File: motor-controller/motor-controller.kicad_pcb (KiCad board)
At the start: 2 copper layers, 65.4 x 35.6 mm, 21 parts, among them J1 Molex 172043-0201 R/A, J2 Molex 172043-0302 R/A, J3 MCU-IO, U1 DRV10983PWP

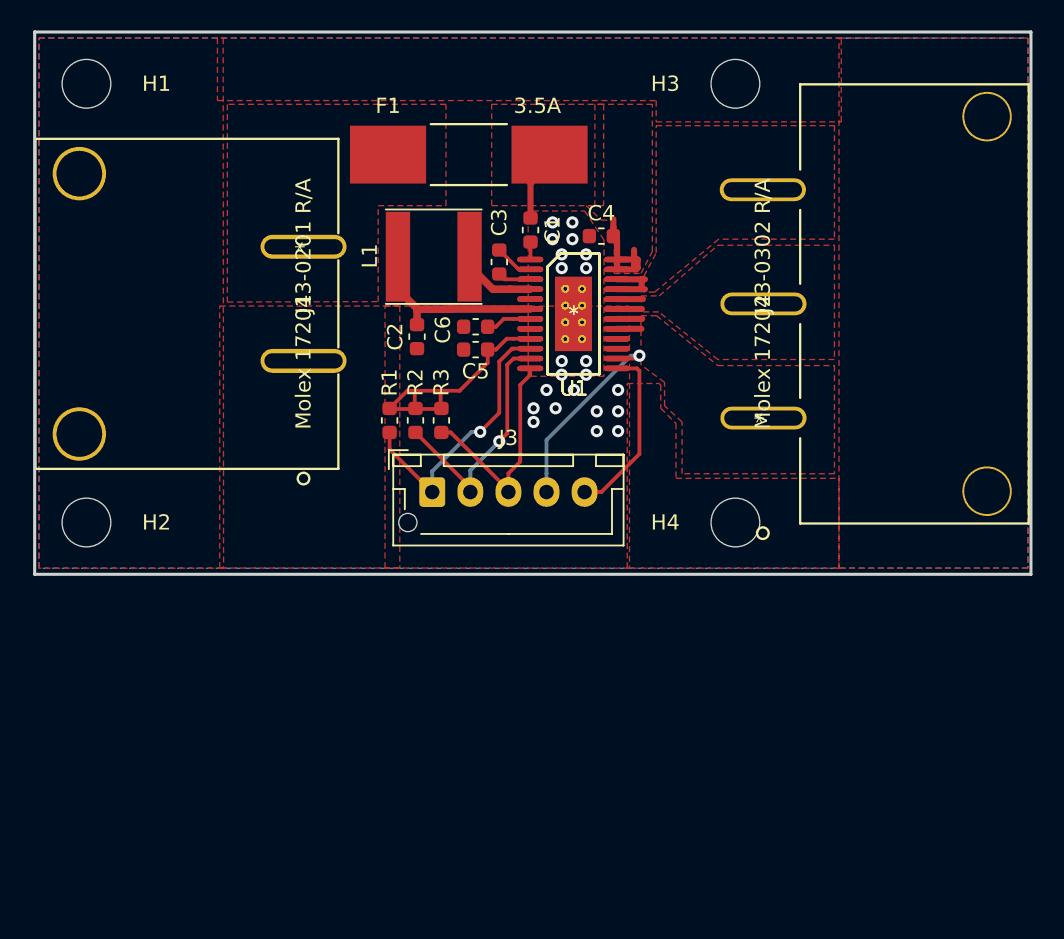
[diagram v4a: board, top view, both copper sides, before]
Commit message: Thermal vias connected to pad in driver IC footprint; added PCB dimensions, adjusted fuse pours.
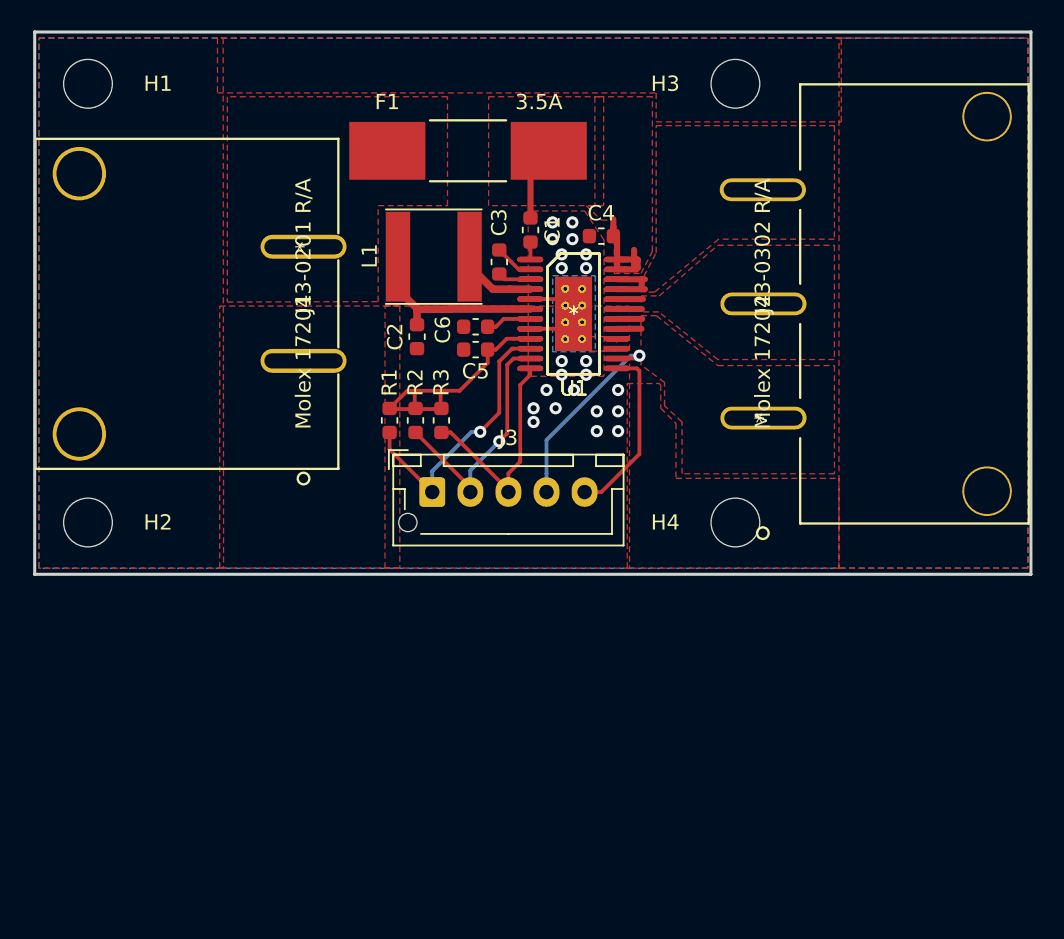
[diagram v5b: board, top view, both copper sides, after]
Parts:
- removed the U1 at (152.4, 103.5) (x3)
- added U1 (x3): DRV10983PWP, custom:PWP0024B, F.Cu at (152.4, 103.5)
- moved F1 0.25 mm to (145.4, 92.8)
- moved H1 0.10 mm to (120.5, 88.4)
- moved H2 0.10 mm to (120.5, 117.2)
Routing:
- net GND: track 0.00 -> 6.51 mm
- net VCC: track 11.8 -> 12.7 mm

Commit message: Prelayout modifications; changed 7-pin connector pinout to permit tighter layout.
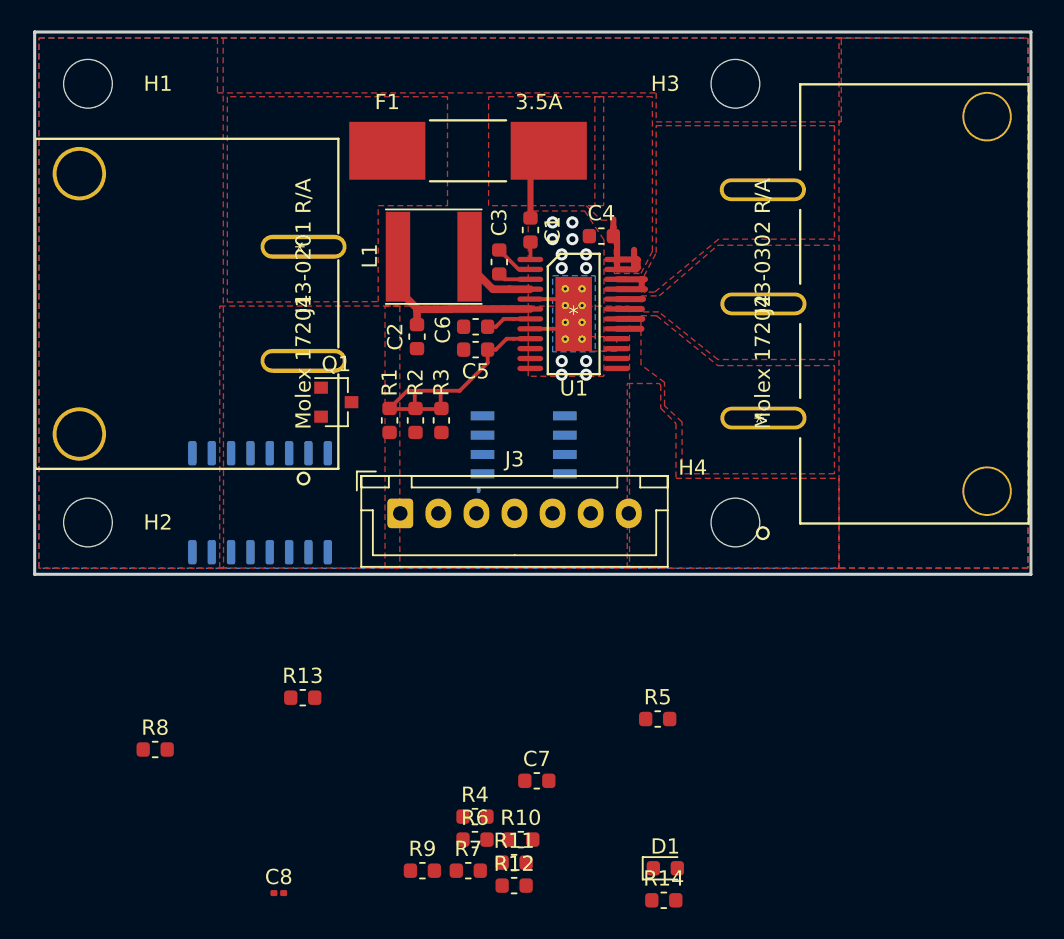
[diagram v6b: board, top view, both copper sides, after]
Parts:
- removed the U1 at (152.4, 103.5) (x3)
- added C7: C, Capacitor_SMD:C_0603_1608Metric, F.Cu at (150.0, 134.2)
- added C8: C, Capacitor_SMD:C_0201_0603Metric, F.Cu at (133.0, 141.5)
- added D1: LED, LED_SMD:LED_0603_1608Metric, F.Cu at (158.4, 139.9)
- added Q1: 2N3904, Package_TO_SOT_SMD:SOT-23, F.Cu at (136.8, 109.3)
- added R10: 4.7k, Resistor_SMD:R_0603_1608Metric, F.Cu at (148.9, 138.0)
- added R11: 4.7k, Resistor_SMD:R_0603_1608Metric, F.Cu at (148.5, 139.5)
- added R12: 4.7k, Resistor_SMD:R_0603_1608Metric, F.Cu at (148.5, 141.0)
- added R13: 4.7k, Resistor_SMD:R_0603_1608Metric, F.Cu at (134.6, 128.7)
- added R14: 220, Resistor_SMD:R_0603_1608Metric, F.Cu at (158.3, 142.0)
- added R4: 75, Resistor_SMD:R_0603_1608Metric, F.Cu at (145.9, 136.5)
- added R5: 200, Resistor_SMD:R_0603_1608Metric, F.Cu at (157.9, 130.1)
- added R6: 200, Resistor_SMD:R_0603_1608Metric, F.Cu at (145.9, 138.0)
- added R7: 200, Resistor_SMD:R_0603_1608Metric, F.Cu at (145.5, 140.1)
- added R8: 75, Resistor_SMD:R_0603_1608Metric, F.Cu at (124.9, 132.1)
- added R9: 1k, Resistor_SMD:R_0603_1608Metric, F.Cu at (142.5, 140.1)
- added U1: DRV10983PWP, custom:PWP0024B, F.Cu at (152.4, 103.5)
- added U2: TLP291-4, Package_SO:SOIC-16_4.55x10.3mm_P1.27mm, B.Cu at (131.8, 115.9)
- added U3: SI8600AC, Package_SO:SOIC-8_3.9x4.9mm_P1.27mm, B.Cu at (149.1, 112.1)
- J3: footprint Connector_JST:JST_XH_B05B-XH-AM_1x05_P2.50mm_Vertical -> Connector_JST:JST_XH_B07B-XH-A_1x07_P2.50mm_Vertical
- moved J3 2.52 mm to (141.0, 116.6)
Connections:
- J3 pad 1: Net-(J3-Pad1) -> /SPEED-uC
- J3 pad 2: Net-(J3-Pad2) -> /FG-uC
- J3 pad 3: Net-(J3-Pad3) -> /DIR-uC
- J3 pad 4: /DIR -> +5V
- J3 pad 5: /SPEED -> GNDD
- R1 pad 2: Net-(J3-Pad1) -> /SDA-MTR
- R2 pad 2: Net-(J3-Pad2) -> /SCL-MTR
- R3 pad 2: Net-(J3-Pad3) -> /FG-MTR
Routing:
- net Net-(J3-Pad1): track 18.2 -> 0.00 mm, vias 1 -> 0
- net Net-(J3-Pad2): track 16.6 -> 0.12 mm, vias 1 -> 0
- net Net-(J3-Pad3): track 14.8 -> 0.00 mm
- net /DIR: track 13.4 -> 0.00 mm, vias 1 -> 0
- net /SPEED: track 11.6 -> 0.00 mm
- net GND: vias 22 -> 12

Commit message: Added in isolator traces and placed resistors; need to add ground planes and tweak layout.
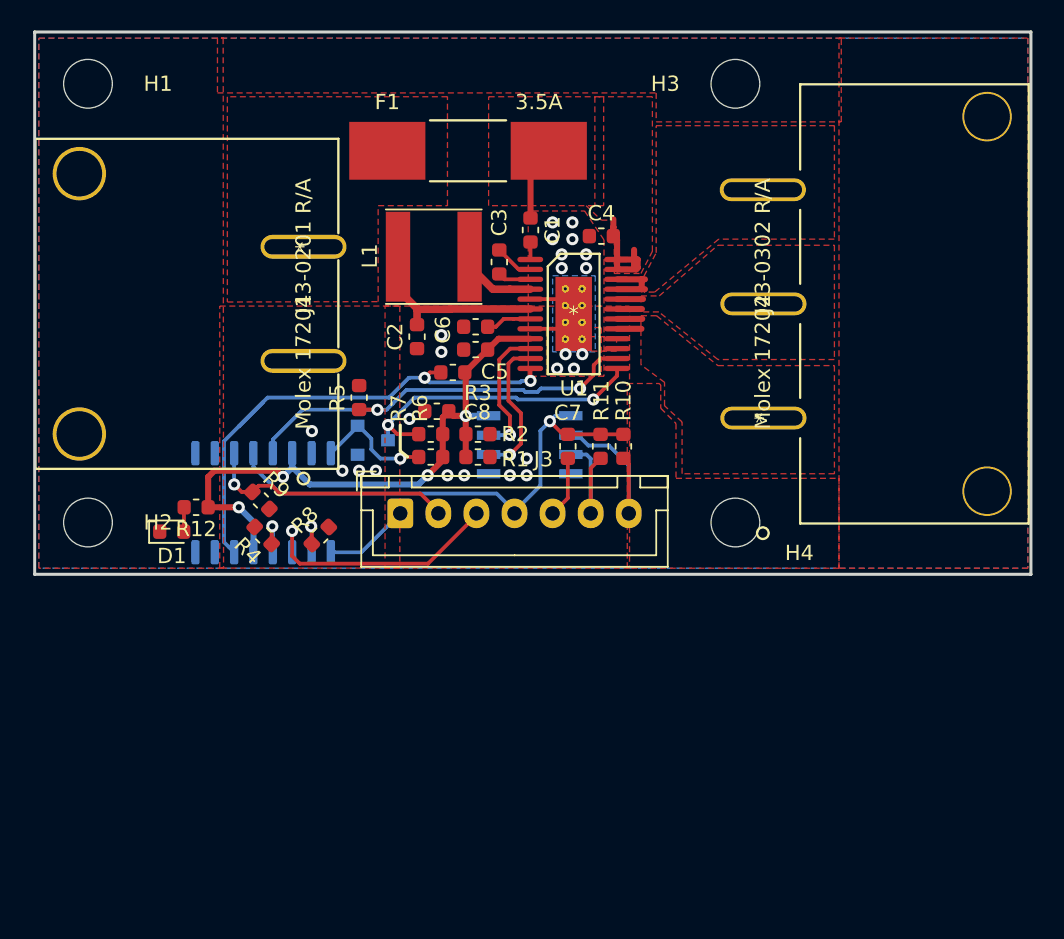
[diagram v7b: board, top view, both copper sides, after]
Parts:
- removed R13: 4.7k, Resistor_SMD:R_0603_1608Metric
- removed R14: 220, Resistor_SMD:R_0603_1608Metric
- C8: footprint Capacitor_SMD:C_0201_0603Metric -> Capacitor_SMD:C_0603_1608Metric
- Q1: moved to B.Cu
- R12: value 4.7k -> 220
- moved D1 39.2 mm to (126.0, 117.8)
- moved C8 33.3 mm to (143.4, 109.9), turned to 180 degrees
- moved R12 32.4 mm to (127.6, 116.2), turned to 180 degrees
- moved R5 28.8 mm to (138.3, 109.0), turned to 90 degrees
- moved R11 27.9 mm to (154.2, 112.2), turned to 270 degrees
- moved R7 27.3 mm to (143.0, 112.9), turned to 180 degrees
- moved R6 26.8 mm to (143.0, 111.4), turned to 180 degrees
- moved R10 26.7 mm to (155.7, 112.2), turned to 270 degrees
- moved R9 26.5 mm to (131.8, 115.8), turned to 315 degrees
- moved R4 23.1 mm to (132.0, 118.0), turned to 135 degrees
- moved C7 22.0 mm to (152.0, 112.2), turned to 270 degrees
- moved R8 17.7 mm to (135.8, 118.0), turned to 45 degrees
- moved R1 6.28 mm to (146.1, 112.9), turned to 0 degrees
- moved R2 4.20 mm to (146.1, 111.4), turned to 0 degrees
- moved Q1 3.47 mm to (139.2, 111.8)
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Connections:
- R12 pad 2: /SCL-MTR -> Net-(D1-Pad2)
- U2 pad 11: /DIR-MTR -> /FG-uC
- U2 pad 12: +3V3 -> +5V
- U2 pad 13: /FG-uC -> /DIR-MTR
- U2 pad 14: +5V -> +3V3
- U2 pad 3: +3V3 -> /DIR-uC
- U2 pad 4: /FG-MTR -> Net-(R4-Pad1)
- U2 pad 5: /DIR-uC -> +3V3
- U2 pad 6: Net-(R4-Pad1) -> /FG-MTR
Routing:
- net /FG-MTR: track 0.00 -> 34.2 mm, vias 0 -> 2
- net +5V: track 0.00 -> 33.0 mm, vias 0 -> 1
- net /DIR-MTR: track 0.00 -> 27.4 mm, vias 0 -> 2
- net +3V3: track 17.5 -> 43.6 mm, vias 0 -> 4
- net /SPEED-MTR: track 0.00 -> 20.3 mm, vias 0 -> 2
- net /DIR-uC: track 0.00 -> 16.8 mm, vias 0 -> 1
- net /FG-uC: track 0.00 -> 16.6 mm, vias 0 -> 1
- net /SCL-uC: track 0.00 -> 11.5 mm
- net /SDA-MTR: track 0.00 -> 9.62 mm, vias 0 -> 1
- net /SCL-MTR: track 0.00 -> 9.00 mm, vias 0 -> 1
- net /SDA-uC: track 0.00 -> 8.89 mm
- net Net-(Q1-Pad2): track 0.00 -> 7.88 mm, vias 0 -> 1
- net /SPEED-uC: track 0.00 -> 5.66 mm
- net GNDD: track 0.00 -> 4.03 mm
- net Net-(R4-Pad1): track 0.00 -> 2.89 mm, vias 0 -> 1
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
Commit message: Added in uC-side ground planes; adjusted isolator trace layouts to pass DRC
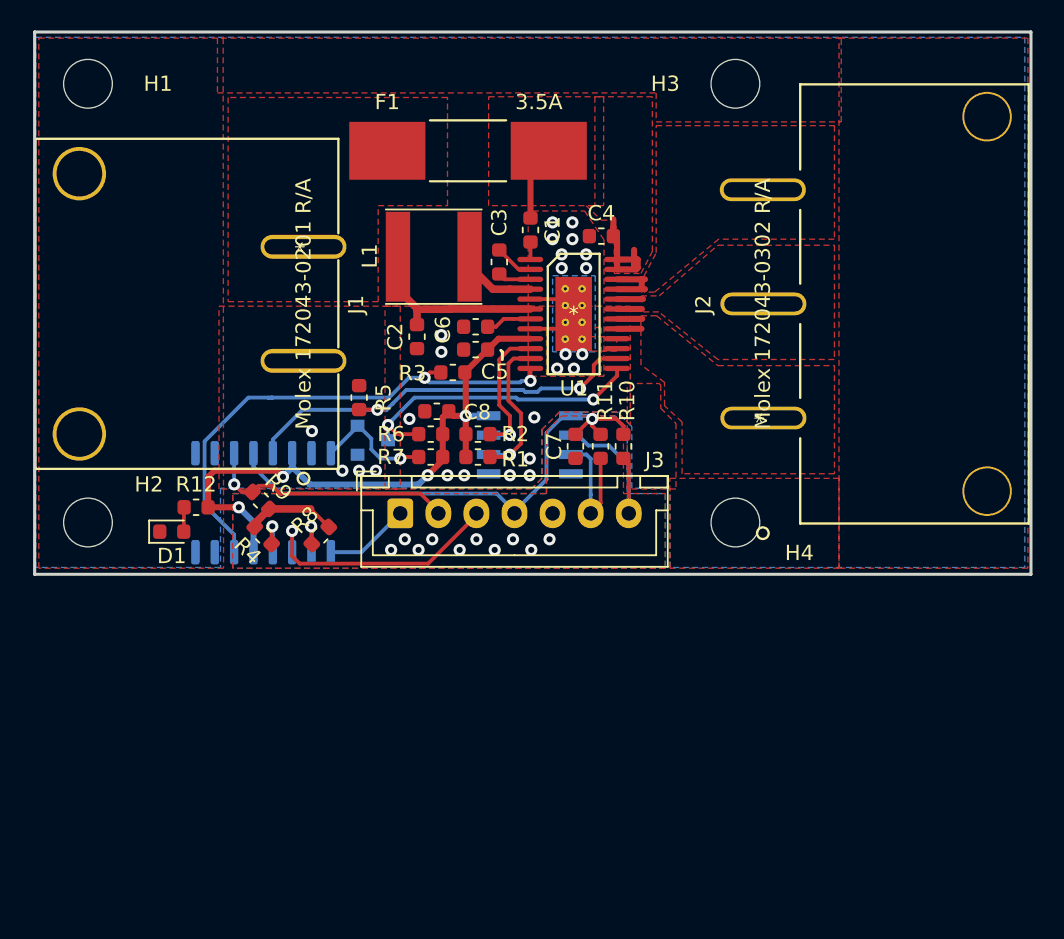
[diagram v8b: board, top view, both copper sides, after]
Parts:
- C7, C8: value C -> 0.1u
- moved C7 0.50 mm to (152.5, 112.2)
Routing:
- net GNDD: track 4.03 -> 5.98 mm, vias 0 -> 10
- net +5V: track 33.0 -> 34.5 mm
- net /SDA-MTR: track 9.62 -> 11.0 mm
- net /SCL-MTR: track 9.00 -> 10.3 mm
- net GND: vias 24 -> 25
- added copper zone on B.Cu, net GNDD
- added copper zone on F.Cu, net GNDD
